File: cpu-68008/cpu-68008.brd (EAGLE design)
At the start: 96.8 x 100 mm, 54 parts, among them IC1 68008, IC11 NE555, IC2 AS6C4008, IC3 39SF010, IC4 DS1244Y, IC5 XR68C681, Q1 8MHz, Q2 3.6864MHz

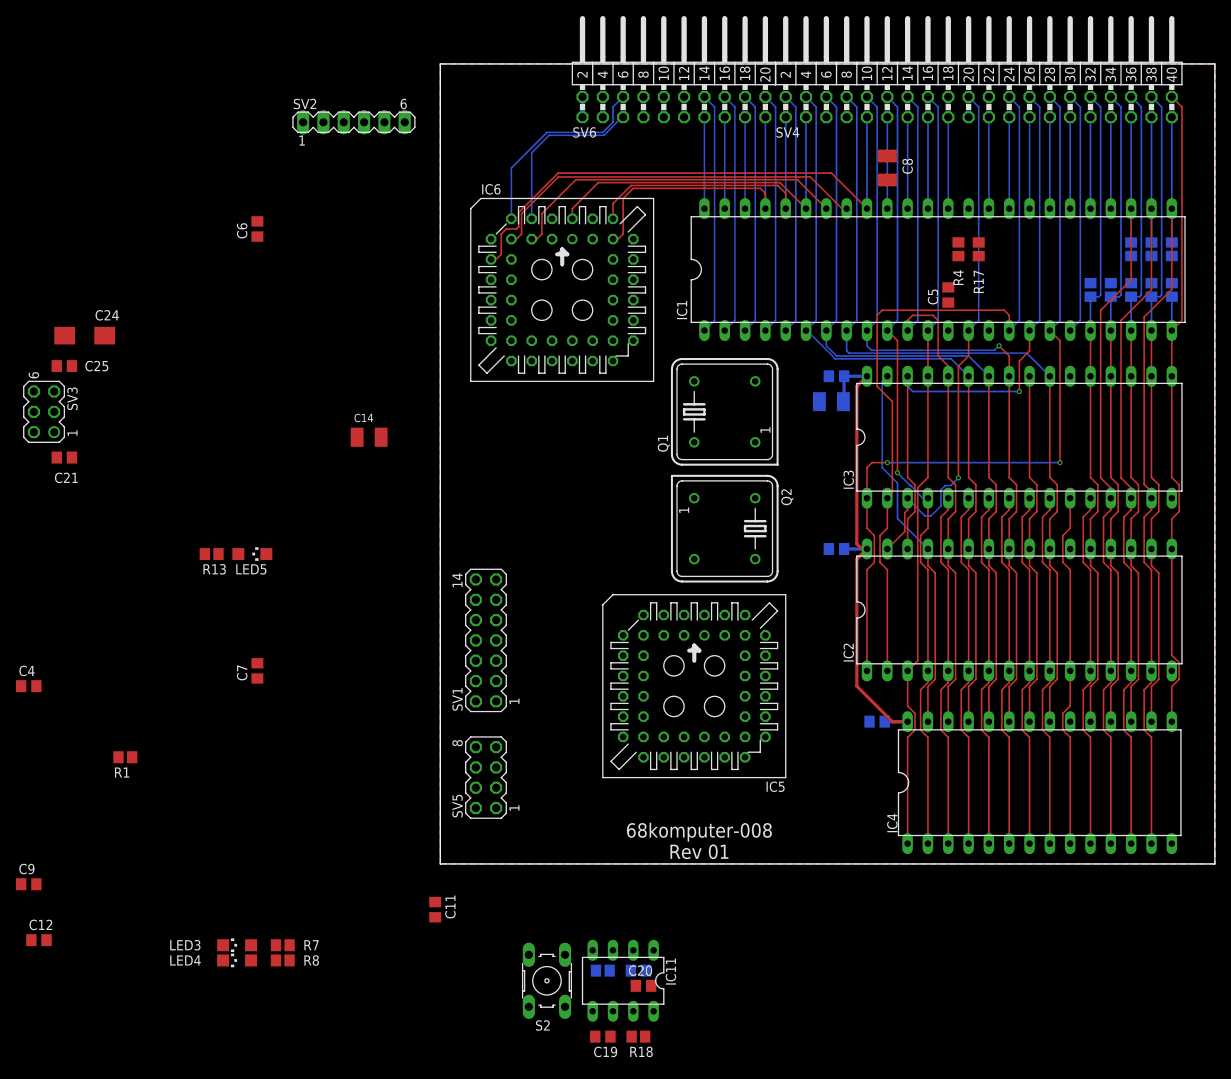
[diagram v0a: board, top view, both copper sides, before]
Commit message: more stuff got routed for 68008
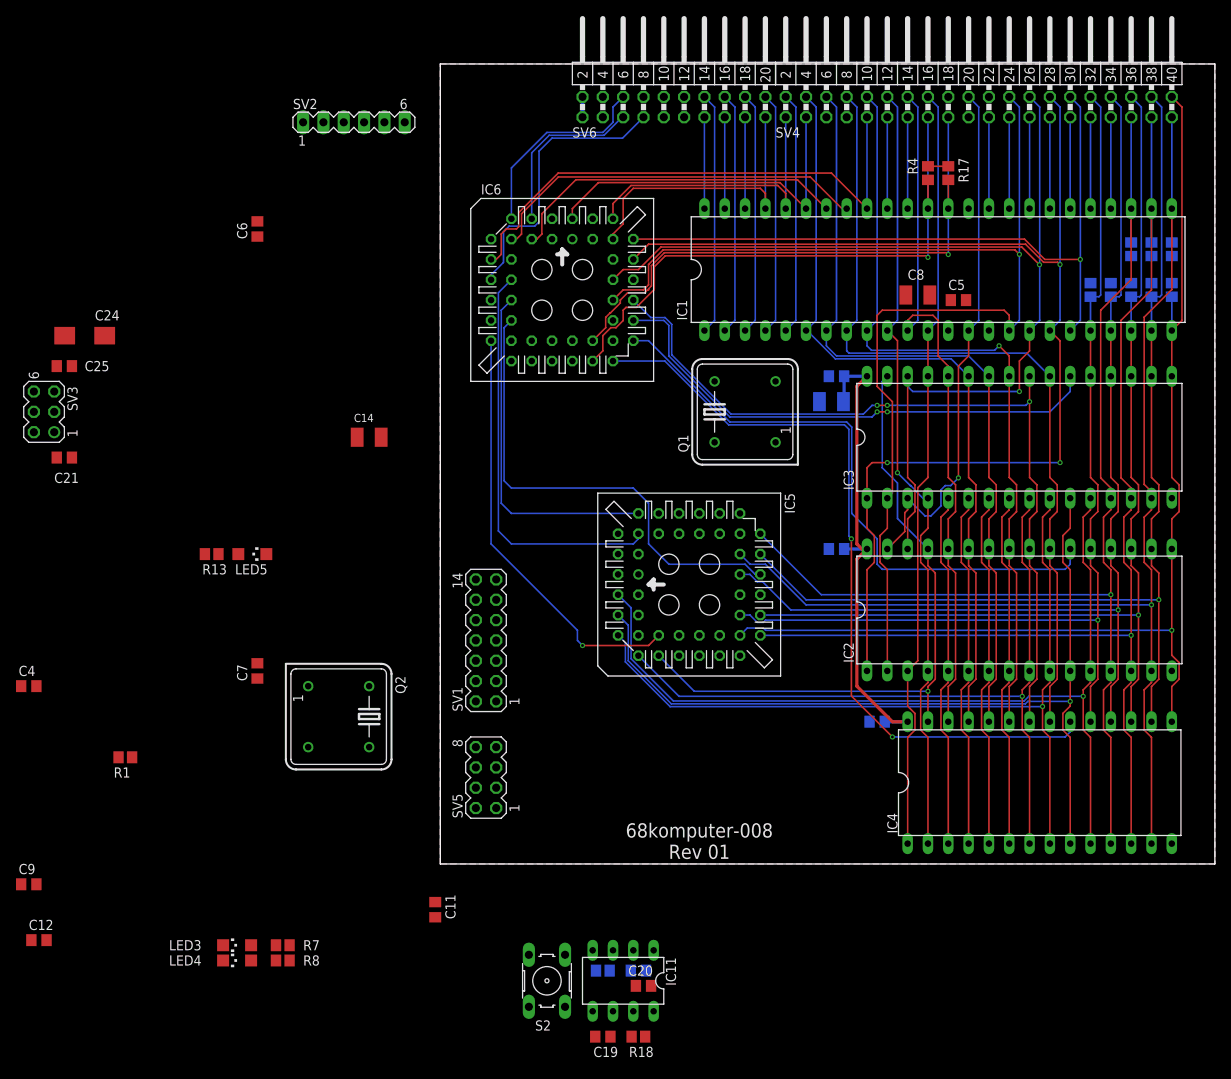
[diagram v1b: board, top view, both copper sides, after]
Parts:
- moved Q2 53.7 mm to (-12.7, 18.4)
- moved C8 16.3 mm to (59.7, 71.1), turned to 180 degrees
- moved IC5 12.7 mm to (31.1, 34.9), turned to 90 degrees
- moved R17 10.3 mm to (63.5, 86.4), turned to 90 degrees
- moved R4 10.3 mm to (61.0, 86.4), turned to 90 degrees
- moved Q1 2.54 mm to (38.1, 56.5)
- moved C5 1.42 mm to (64.8, 70.5), turned to 0 degrees
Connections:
- removed net 68681_IRQ: IC5.24
- new net !68681_IRQ: IC5.24, IC6.16
- new net !BUS_CS: IC6.11, SV6.7
- net !68681_CS: now also IC6.14
- net !68681_DTACK: now also IC6.17
- net !68681_IACK: now also IC6.12
- net !AS: now also IC6.24
- net !DTACK: now also IC6.20
- net !HALT: now also IC6.27
- net !OE: now also IC6.33
- net !RAM_CS: now also IC6.29
- net !RESET: now also IC6.26
- net !ROM_CS: now also IC6.31
- net !RTC_CS: now also IC6.28
- net A15: now also IC6.21
- net A16: now also IC6.34
- net A17: now also IC6.36
- net A18: now also IC6.37
- net A19: now also IC6.39
- net CPLD_TCK: now also IC6.32
- net CPLD_TDI: now also IC6.7
- net CPLD_TDO: now also IC6.38
- net CPLD_TMS: now also IC6.13
- net R/!W!: now also IC6.25
- net RESET: now also IC6.1
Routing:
- net !RTC_CS: track 0.00 -> 97.5 mm, vias 0 -> 2
- net !RAM_CS: track 0.00 -> 76.8 mm
- net A0: track 56.1 -> 123.7 mm, vias 0 -> 1
- net !ROM_CS: track 0.00 -> 65.1 mm, vias 0 -> 2
- net A1: track 56.1 -> 120.0 mm, vias 0 -> 1
- net !HALT: track 11.4 -> 72.4 mm, vias 0 -> 1
- net !RESET: track 11.4 -> 72.1 mm, vias 0 -> 1
- net !68681_IRQ: track 0.00 -> 60.3 mm
- net !OE: track 44.7 -> 103.0 mm, vias 0 -> 3
- net A2: track 56.1 -> 114.3 mm, vias 0 -> 1
- net A19: track 30.3 -> 87.2 mm, vias 0 -> 1
- net A17: track 76.3 -> 132.2 mm, vias 1 -> 2
- net A18: track 97.8 -> 153.0 mm, vias 2 -> 3
- net A16: track 95.5 -> 150.6 mm, vias 0 -> 1
- net D3: track 84.9 -> 139.4 mm, vias 0 -> 1
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
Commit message: finished routing CPLD
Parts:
- moved C12 112.5 mm to (27.3, 72.0), flipped to the bottom, turned to 270 degrees
- moved C18 104.0 mm to (-8.89, 85.1)
- moved R16 104.0 mm to (-13.3, 85.1)
- moved C19 104.0 mm to (-13.3, 76.8)
- moved C20 104.0 mm to (-8.26, 83.2)
- moved IC11 104.0 mm to (-10.8, 83.8)
- moved R18 104.0 mm to (-8.89, 76.8)
- moved S2 104.0 mm to (-20.3, 83.8)
- moved C9 88.9 mm to (3.81, 67.1), flipped to the bottom, turned to 270 degrees
- moved C6 66.5 mm to (38.1, 52.7), flipped to the bottom, turned to 180 degrees
- moved C11 51.5 mm to (-8.89, 45.1)
- moved SV2 46.7 mm to (17.1, 55.2)
- moved C4 37.4 mm to (-15.2, 31.8)
- moved R1 36.0 mm to (-12.7, 37.5)
- moved C14 32.4 mm to (15.9, 74.3), flipped to the bottom, turned to 180 degrees
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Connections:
- net !AS: now also IC6.27; no longer IC6.24
- net !DTACK: now also IC6.36; no longer IC6.20
- net !HALT: now also IC6.37; no longer IC6.27
- net !RESET: now also IC6.39; no longer IC6.26
- net A15: now also IC6.26; no longer IC6.21
- net A16: now also IC6.25; no longer IC6.34
- net A17: now also IC6.24; no longer IC6.36
- net A18: now also IC6.21; no longer IC6.37
- net A19: now also IC6.20; no longer IC6.39
- net R/!W!: now also IC6.34; no longer IC6.25
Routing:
- net +5V: track 65.7 -> 290.3 mm, vias 0 -> 3
- net !AS: track 11.4 -> 83.8 mm
- net CLK: track 11.4 -> 82.2 mm, vias 0 -> 1
- net R/!W!: track 93.5 -> 155.4 mm
- net !DTACK: track 11.4 -> 69.7 mm
- net A15: track 67.0 -> 123.7 mm, vias 1 -> 2
- net CPLD_TDI: track 0.00 -> 35.3 mm
- net CPLD_TDO: track 0.00 -> 23.2 mm, vias 0 -> 2
- net A18: track 153.0 -> 175.5 mm
- net CPLD_TMS: track 0.00 -> 22.2 mm
- net A19: track 87.2 -> 108.7 mm
- net !RESET: track 72.1 -> 54.9 mm, vias 1 -> 0
- net !HALT: track 72.4 -> 57.3 mm, vias 1 -> 0
- net CPLD_TCK: track 0.00 -> 14.5 mm
- net A16: track 150.6 -> 162.6 mm
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
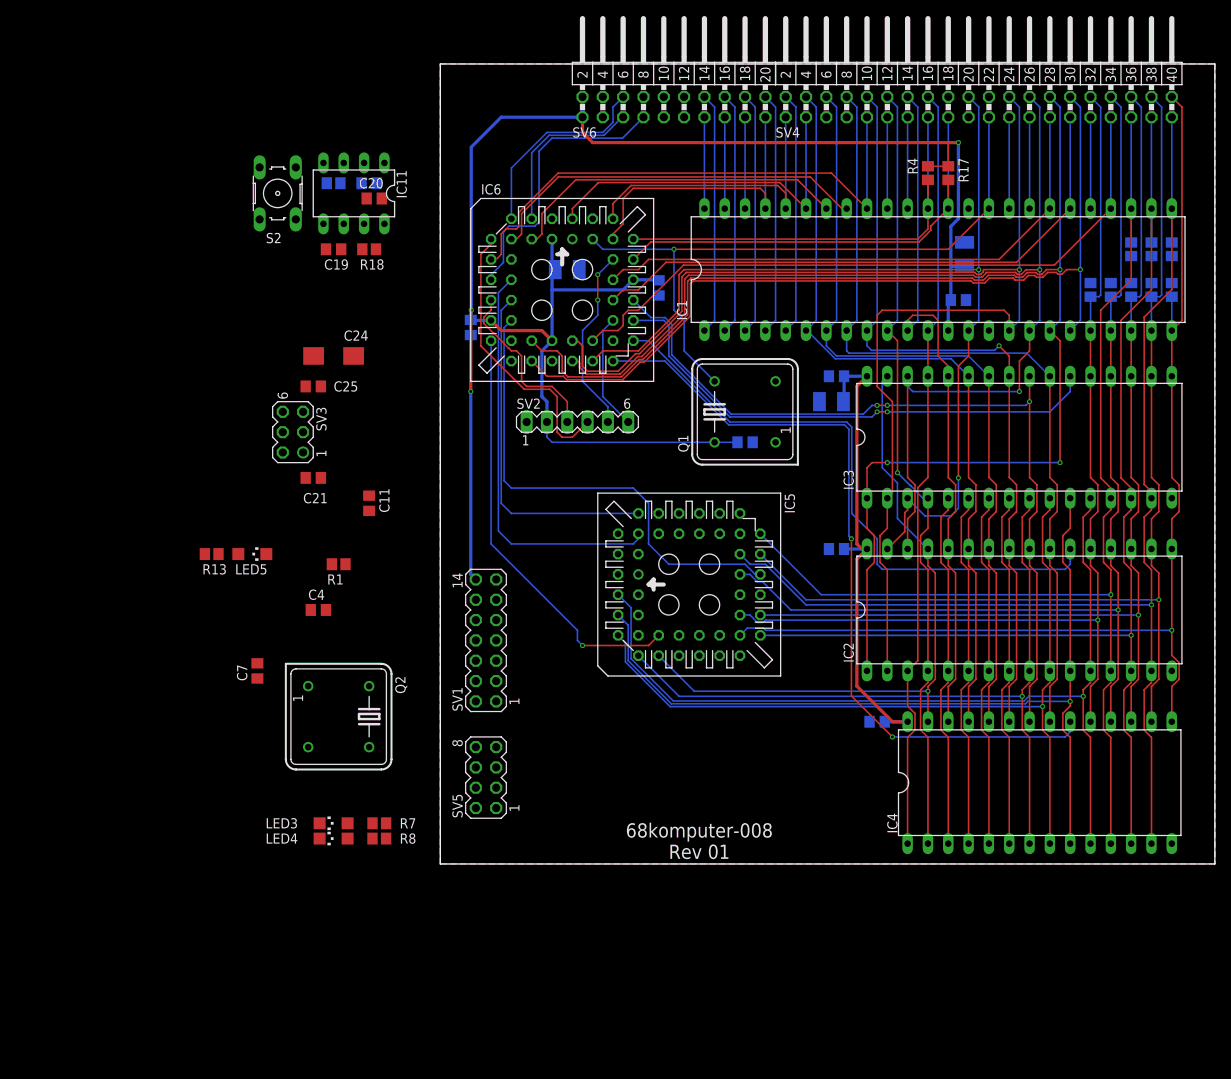
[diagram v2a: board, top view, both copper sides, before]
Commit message: routed duart IO and serial channels
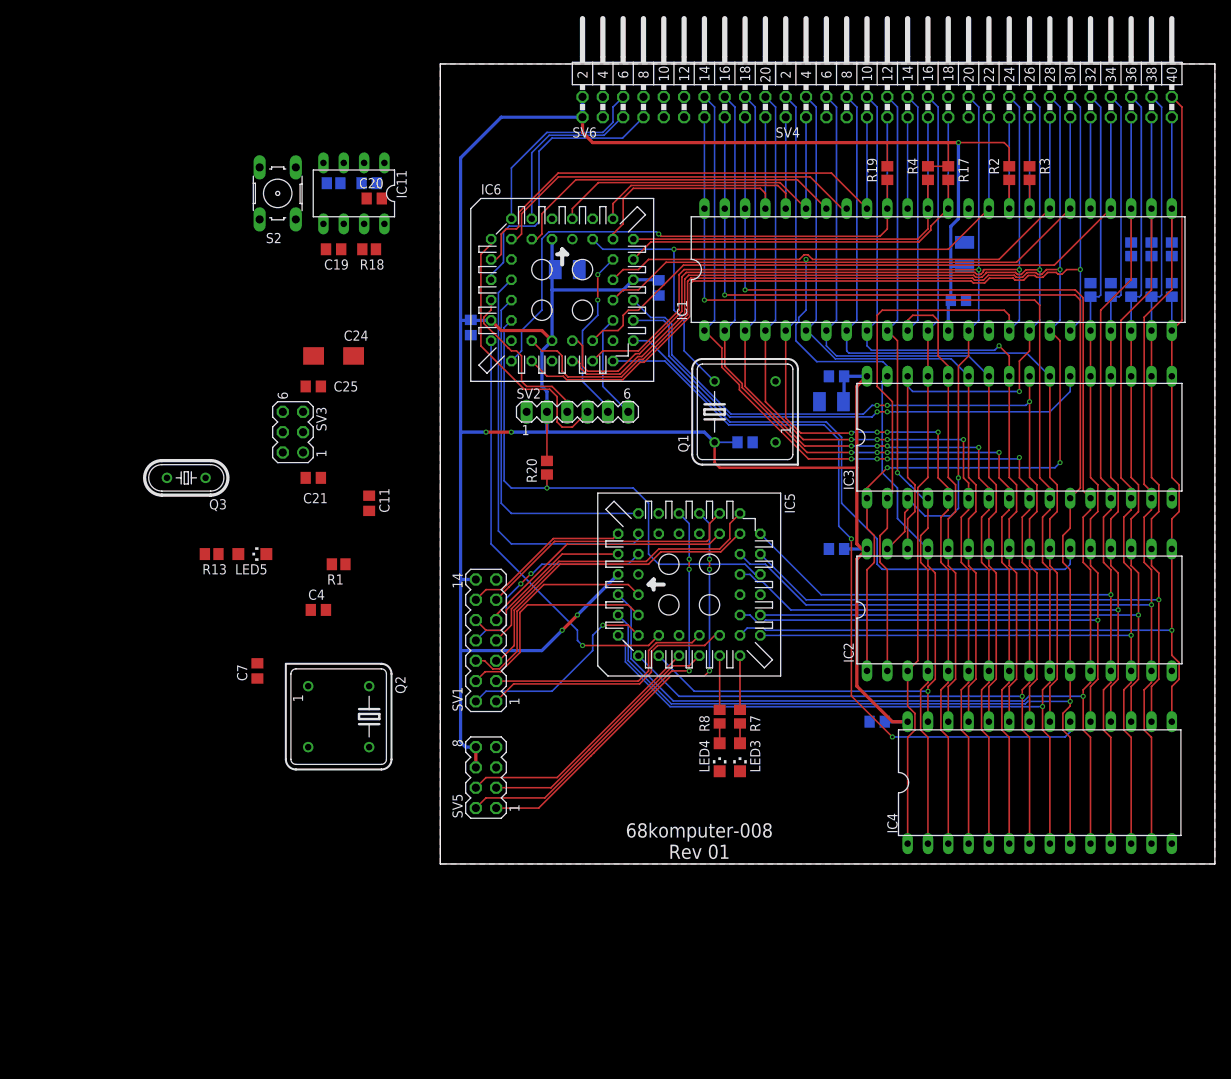
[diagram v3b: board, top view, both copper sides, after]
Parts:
- added Q3: (no value), crystal:HC49/S
- added R19, R2, R20, R3: 10k, rcl:R2012
- moved LED3 51.5 mm to (37.5, 13.3), turned to 180 degrees
- moved LED4 49.3 mm to (34.9, 13.3), turned to 180 degrees
- moved R7 47.0 mm to (37.5, 18.4), turned to 270 degrees
- moved R8 45.2 mm to (34.9, 18.4), turned to 270 degrees
- moved SV2 1.27 mm to (17.1, 56.5)
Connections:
- net !68681_IRQ: now also R20.1
- net !BG: now also R3.2
- net !BR: now also R2.2
- net !VPA: now also IC6.18, R19.2
- net +5V: now also R19.1, R2.1, R20.2
- net GND: now also R3.1, SV6.10, SV6.11, SV6.12, SV6.8, SV6.9
- net IO_IN0: now also IC5.40; no longer IC5.8
- net IO_IN1: now also IC5.42; no longer IC5.5
- net IO_IN2: now also IC5.43; no longer IC5.40
- net IO_IN4: now also IC5.5; no longer IC5.43
- net IO_IN5: now also IC5.8; no longer IC5.42
- net IO_OUT0: now also IC5.31; no longer IC5.32
- net IO_OUT1: now also IC5.32; no longer IC5.14
- net IO_OUT2: now also IC5.29; no longer IC5.31
- net IO_OUT3: now also IC5.30; no longer IC5.15
- net IO_OUT4: now also IC5.14; no longer IC5.30
- net STATUS0: now also IC5.15; no longer IC5.29
- net UART0_RX: now also SV5.2; no longer SV5.4
- net UART0_TX: now also SV5.1; no longer SV5.3
- net UART1_RX: now also SV5.4; no longer SV5.2
- net UART1_TX: now also SV5.3; no longer SV5.1
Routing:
- net +5V: track 290.3 -> 390.2 mm, vias 3 -> 5
- net A1: track 120.0 -> 200.8 mm, vias 1 -> 2
- net A0: track 123.7 -> 202.0 mm, vias 1 -> 2
- net A2: track 114.3 -> 192.6 mm, vias 1 -> 2
- net !VPA: track 11.4 -> 78.6 mm, vias 0 -> 1
- net UART0_RX: track 0.00 -> 54.0 mm, vias 0 -> 3
- net UART0_TX: track 0.00 -> 54.0 mm, vias 0 -> 3
- net A3: track 125.0 -> 178.5 mm, vias 1 -> 5
- net A4: track 75.0 -> 124.7 mm, vias 0 -> 4
- net A5: track 75.0 -> 121.2 mm, vias 0 -> 4
- net A6: track 75.0 -> 118.2 mm, vias 0 -> 4
- net IO_OUT3: track 0.00 -> 39.7 mm
- net A7: track 75.0 -> 114.5 mm, vias 0 -> 4
- net IO_OUT2: track 0.00 -> 39.4 mm
- net IO_OUT0: track 0.00 -> 33.5 mm
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
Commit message: cleaned up routing for duart, added new duart clock circuit
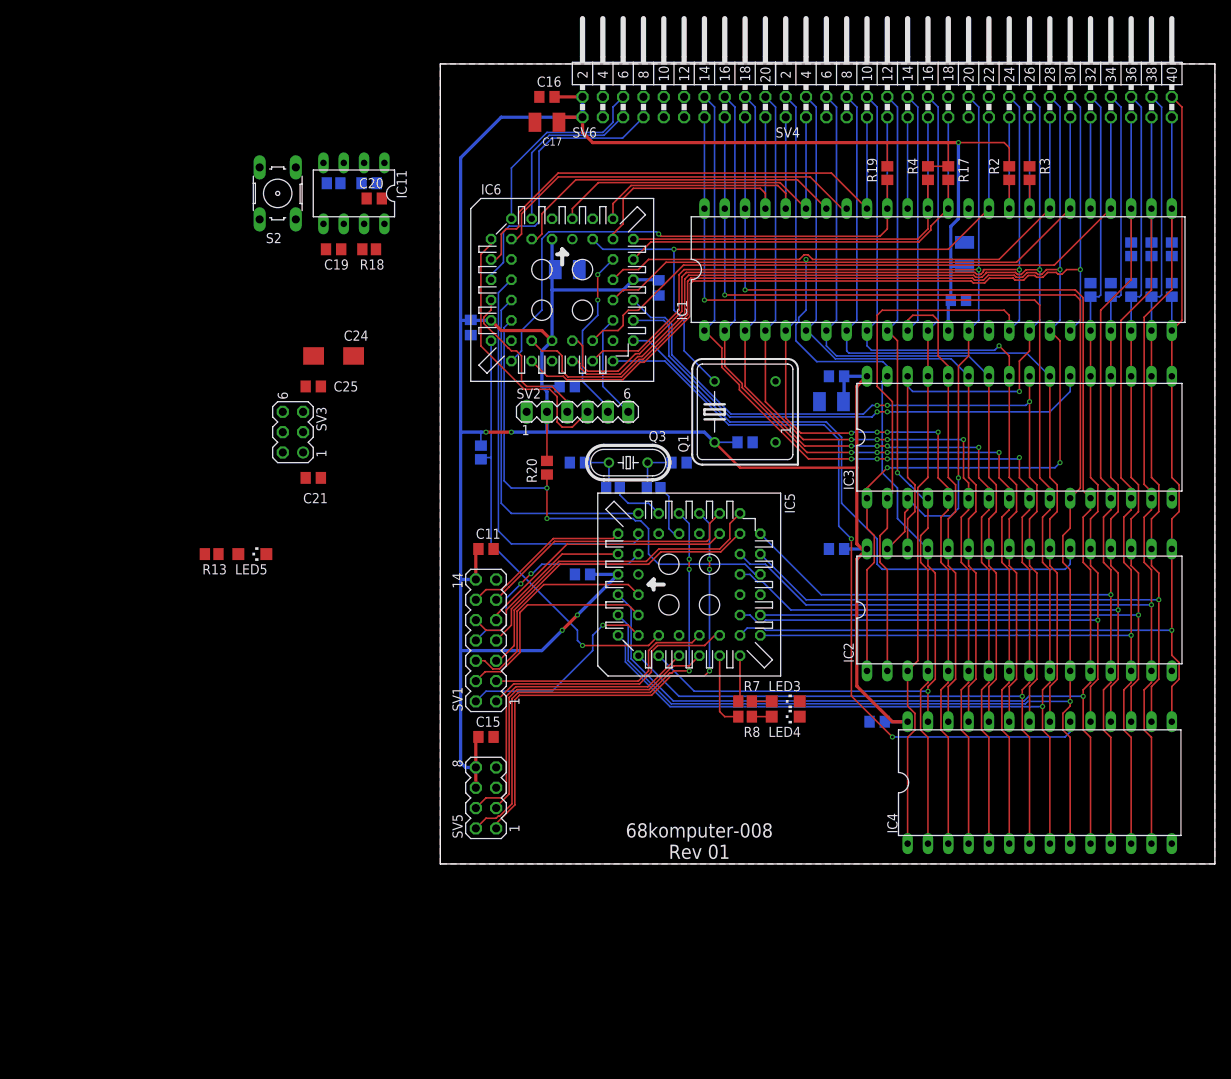
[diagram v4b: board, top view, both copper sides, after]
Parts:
- removed Q2: 3.6864MHz, crystal:DIL08S
- added C13: 27pF, rcl:C0805
- added C15, C16, C22: 100nF, rcl:C0805
- added C17: 10µF, rcl:SMC_B
- added R21, R22: 100R, rcl:R2012
- C7: value 100nF -> 27pF
- Q3: value (none) -> 3.6864 MHz
- moved C7 58.8 mm to (29.8, 50.2), flipped to the bottom, turned to 0 degrees
- moved Q3 55.3 mm to (23.5, 50.2)
- moved C4 33.3 mm to (17.8, 36.2), flipped to the bottom
- moved R1 22.6 mm to (5.08, 51.4), flipped to the bottom, turned to 90 degrees
- moved C11 15.7 mm to (5.71, 39.4), turned to 0 degrees
- moved LED4 9.69 mm to (43.2, 18.4), turned to 270 degrees
- moved LED3 9.03 mm to (43.2, 20.3), turned to 270 degrees
- moved R8 3.18 mm to (38.1, 18.4), turned to 0 degrees
- moved SV5 2.54 mm to (5.71, 8.26)
- moved R7 2.01 mm to (38.1, 20.3), turned to 0 degrees
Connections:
- removed net 68681_CLK: IC5.36, Q2.5
- new net 68681_X1: IC5.36, R22.2
- new net 68681_X2: IC5.37, R21.2
- new net N$2: C7.2, Q3.1, R22.1
- new net N$3: C13.2, Q3.2, R21.1
- net +5V: now also C15.1, C16.1, C17.+, C22.1; no longer C7.1, Q2.8
- net GND: now also C13.1, C15.2, C16.2, C17.-, C22.2, C7.1; no longer C7.2, Q2.4
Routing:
- net +5V: track 390.2 -> 413.4 mm
- net UART0_TX: track 54.0 -> 63.1 mm
- net UART0_RX: track 54.0 -> 62.7 mm
- net UART1_TX: track 32.2 -> 40.4 mm
- net UART1_RX: track 32.2 -> 40.4 mm
- net 68681_X1: track 0.00 -> 7.05 mm
- net 68681_X2: track 0.00 -> 6.68 mm
- net N$3: track 0.00 -> 6.30 mm
- net N$2: track 0.00 -> 6.20 mm
- net STATUS0: track 6.77 -> 9.57 mm
- net !68681_DTACK: track 52.9 -> 54.2 mm
- net STATUS1: track 6.77 -> 5.80 mm
- net !68681_IRQ: track 62.7 -> 63.1 mm, vias 1 -> 2
